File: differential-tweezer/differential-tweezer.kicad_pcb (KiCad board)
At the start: 4 copper layers, 32 x 23 mm, 64 parts, among them J1 5V, J2 IN+, J3 Conn_Coaxial, J4 IN-, J5 Power, U1 R1283B, U2 OPA810, U3 OPA810, U4 OPA810

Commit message: Revision 2
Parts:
- removed C11: 100nF, Capacitor_SMD:C_0603_1608Metric
- removed C18: 22nF, Capacitor_SMD:C_0603_1608Metric
- removed FID1, FID2, FID3, FID4: Fiducial_0.5mm_Mask1mm, Fiducial:Fiducial_0.5mm_Mask1mm
- removed R8: 470, Resistor_SMD:R_0603_1608Metric
- removed RV3: 47k, Potentiometer_SMD:Potentiometer_Bourns_TC33X_Vertical
- removed SLOT1, SLOT2: SLOT_5x1, oscilloscope-probes:SLOT_5x1
- added C24: 100nF, Capacitor_SMD:C_0603_1608Metric, F.Cu at (88.0, 144.5)
- added C25: 100nF, Capacitor_SMD:C_0603_1608Metric, F.Cu at (94.8, 142.3)
- added C26: 10µF, Capacitor_SMD:C_0603_1608Metric, F.Cu at (78.9, 147.9)
- added H1: 2.2mm, MountingHole:MountingHole_2.2mm_M2_DIN965_Pad, F.Cu at (89.4, 149.7)
- added J6: Probe-, oscilloscope-probes:TE_2306454_LEFT, F.Cu at (72.9, 128.2)
- added L8: 1k, Inductor_SMD:L_0603_1608Metric, F.Cu at (73.3, 136.9)
- added R16: 22, Resistor_SMD:R_0603_1608Metric, F.Cu at (89.7, 125.8)
- added R17: 22, Resistor_SMD:R_0603_1608Metric, F.Cu at (75.8, 127.0)
- added R18: 110, Resistor_SMD:R_0603_1608Metric, F.Cu at (91.3, 118.5)
- added R19: 110, Resistor_SMD:R_0603_1608Metric, F.Cu at (78.1, 118.3)
- added R20: 220, Resistor_SMD:R_0603_1608Metric, F.Cu at (94.8, 143.8)
- added R21: 220, Resistor_SMD:R_0603_1608Metric, F.Cu at (93.7, 146.0)
- added R22: 49.9, Resistor_SMD:R_0603_1608Metric, F.Cu at (87.3, 141.6)
- added SW1: GAIN, oscilloscope-probes:78HF01GWRT, F.Cu at (84.0, 131.2)
- added TP1: +5V, TestPoint:TestPoint_Pad_D2.5mm, B.Cu at (93.9, 148.9)
- added TP2: +6V, TestPoint:TestPoint_Pad_D2.5mm, B.Cu at (81.1, 136.1)
- added TP3: -6V, TestPoint:TestPoint_Pad_D2.5mm, B.Cu at (81.1, 139.7)
- added TP4: GND, TestPoint:TestPoint_Pad_D2.5mm, B.Cu at (78.0, 142.0)
- C1, C12, C2, C9: footprint Capacitor_SMD:C_0805_2012Metric -> Capacitor_SMD:C_0603_1608Metric; moved to F.Cu
- C10: value 10µF -> 100nF; footprint Capacitor_SMD:C_0805_2012Metric -> Capacitor_SMD:C_0603_1608Metric; moved to F.Cu
- C13, C6, C7: value 100nF -> 10µF
- C14, C15: value 100nF -> 20pF
- C16, C17: value 10µF -> 8-30pF; footprint Capacitor_SMD:C_0805_2012Metric -> Capacitor_SMD:C_Trimmer_Murata_TZC3; moved to F.Cu
- C19: value 2pF -> N/A
- C20, C22, C23: value 6pF -> 100nF; footprint Capacitor_SMD:C_Trimmer_Murata_TZC3 -> Capacitor_SMD:C_0603_1608Metric
- C21: value 2pF -> 100nF
- C3: value 100nF -> 10µF; moved to F.Cu
- C4: value 10µF -> 100pF; footprint Capacitor_SMD:C_0805_2012Metric -> Capacitor_SMD:C_0603_1608Metric; moved to F.Cu
- C5: value 100nF -> 100pF
- C8: value 22nF -> 10µF; moved to F.Cu
- D1, D2: value BAT54 -> NSR05T30; footprint Diode_SMD:D_SOD-123 -> Diode_SMD:D_SOD-523; moved to F.Cu
- J1: value 5V -> Triax; footprint oscilloscope-probes:WIREPAD_WIDE -> oscilloscope-probes:TRIAX_TUBE
- J2: value IN+ -> Input; footprint oscilloscope-probes:SOLDERPAD_3x1.5 -> oscilloscope-probes:Tensility_54-00177
- J3: value Conn_Coaxial -> Probe+; footprint oscilloscope-probes:COAX_SOLDER -> oscilloscope-probes:TE_2306454_RIGHT
- J4: value IN- -> Probe+_GND; footprint oscilloscope-probes:SOLDERPAD_3x1.5 -> oscilloscope-probes:TE_2306454_RIGHT
- J5: value Power -> Probe-_GND; footprint Connector_PinHeader_2.54mm:PinHeader_1x04_P2.54mm_Vertical -> oscilloscope-probes:TE_2306454_LEFT
- L1, L5, L6, R1, R4, U1: moved to F.Cu
- L2, L7: value 47µH -> 1k; footprint Inductor_SMD:L_Taiyo-Yuden_NR-40xx_HandSoldering -> Inductor_SMD:L_0603_1608Metric; moved to F.Cu
- L3, L4: value 1k -> 4.7µH; footprint Inductor_SMD:L_0603_1608Metric -> Inductor_SMD:L_0805_2012Metric; moved to F.Cu
- R10, R9: value 1M -> 499k
- R12: value 47 -> 475k
- R13: value 470 -> 475k
- R14: value 470 -> 220
- R15: value 1M -> 220
- R2: value 100k -> 4.99k; moved to F.Cu
- R3: value 10k -> 4.99k; moved to F.Cu
- R5: value 100k -> 1k; moved to F.Cu
- R6: value 10k -> 1k; moved to F.Cu
- R7: value 470 -> 10M
- RV1, RV2: value 47k -> 50k
- U2, U3, U4: value OPA810 -> OPA659; footprint Package_TO_SOT_SMD:SOT-23-5 -> Package_SON:Texas_S-PVSON-N8_ThermalVias
- moved L4 27.7 mm to (73.8, 143.2), turned to 90 degrees
- moved C4 27.2 mm to (77.4, 147.9)
- moved C5 27.1 mm to (76.6, 150.2)
- moved J1 26.1 mm to (84.1, 139.8), turned to 90 degrees
- moved C1 25.0 mm to (94.2, 150.5), turned to 270 degrees
- moved C23 24.6 mm to (75.1, 118.3), turned to 270 degrees
- moved R10 24.2 mm to (80.0, 122.9)
- moved L1 23.2 mm to (95.6, 149.0), turned to 90 degrees
- moved C3 22.4 mm to (90.7, 146.1)
- moved C2 22.1 mm to (92.7, 150.5)
- moved C20 21.2 mm to (89.8, 118.5), turned to 90 degrees
- moved C7 21.0 mm to (75.6, 140.7)
- moved L2 21.0 mm to (93.3, 148.2), turned to 180 degrees
- moved L6 20.4 mm to (75.6, 139.2), turned to 180 degrees
- moved J5 20.1 mm to (73.0, 125.5), turned to 87 degrees
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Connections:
- C1 pad 1: Net-(C1-Pad1) -> +5V
- C10 pad 1: Net-(C10-Pad1) -> /OFFSET_TRIM
- C12 pad 1: -12V -> +6V
- C13 pad 1: GND -> -6V
- C13 pad 2: -12V -> GND
- C14 pad 1: GND -> /IN+
- C14 pad 2: -12V -> /CONN_IN+
- C15 pad 1: GND -> /IN-
- C15 pad 2: -12V -> /CONN_IN-
- C16 pad 1: Net-(C16-Pad1) -> /IN+
- C17 pad 1: Net-(C17-Pad1) -> /IN-
- C19 pad 1: GND -> Net-(C19-Pad1)
- C20 pad 1: Net-(C20-Pad1) -> +6V
- C21 pad 1: Net-(C21-Pad1) -> GND
- C21 pad 2: Net-(C21-Pad2) -> -6V
- C22 pad 1: Net-(C22-Pad1) -> +6V
- C23 pad 1: Net-(C23-Pad1) -> GND
- C23 pad 2: Net-(C21-Pad1) -> -6V
- C3 pad 1: Net-(C2-Pad1) -> Net-(C26-Pad1)
- C4 pad 1: +12V -> Net-(C4-Pad1)
- C4 pad 2: GND -> Net-(C4-Pad2)
- C5 pad 1: +12V -> Net-(C5-Pad1)
- C5 pad 2: GND -> Net-(C5-Pad2)
- C6 pad 1: +12V -> Net-(C6-Pad1)
- C7 pad 1: +12V -> Net-(C7-Pad1)
- C8 pad 2: Net-(C8-Pad2) -> GND
- D1 pad 1: Net-(C1-Pad1) -> Net-(D1-Pad1)
- D1 pad 2: Net-(D1-Pad2) -> Net-(C7-Pad1)
- D2 pad 1: Net-(D2-Pad1) -> Net-(C6-Pad1)
- D2 pad 2: Net-(C9-Pad1) -> Net-(D2-Pad2)
- J1 pad 1: Net-(C16-Pad1) -> /OUT
- J3 pad 1: Net-(C23-Pad1) -> /IN+
- J4 pad 1: Net-(C22-Pad1) -> GND
- J5 pad 1: +12V -> GND
- L1 pad 1: Net-(C16-Pad1) -> +5V
- L1 pad 2: Net-(C17-Pad1) -> Net-(C2-Pad1)
- L2 pad 1: Net-(C17-Pad1) -> Net-(C2-Pad1)
- L2 pad 2: Net-(D1-Pad2) -> Net-(C26-Pad1)
- L3 pad 1: Net-(C1-Pad1) -> Net-(C26-Pad1)
- L3 pad 2: Net-(C2-Pad1) -> Net-(D2-Pad2)
- L4 pad 1: Net-(C2-Pad1) -> GND
- L4 pad 2: +12V -> Net-(D1-Pad1)
- L5 pad 1: Net-(C9-Pad1) -> Net-(C6-Pad1)
- L5 pad 2: Net-(C10-Pad1) -> Net-(C8-Pad1)
- L6 pad 1: Net-(C10-Pad1) -> Net-(C7-Pad1)
- L6 pad 2: -12V -> Net-(C9-Pad1)
- L7 pad 1: GND -> Net-(C8-Pad1)
- L7 pad 2: Net-(D2-Pad1) -> +6V
- R1 pad 1: Net-(C8-Pad1) -> Net-(C5-Pad2)
- R1 pad 2: Net-(C1-Pad1) -> Net-(R1-Pad2)
- R10 pad 1: Net-(R10-Pad1) -> /IN-
- R10 pad 2: Net-(C23-Pad1) -> /CONN_IN-
- R12 pad 1: Net-(C23-Pad1) -> /IN+
- R12 pad 2: Net-(C21-Pad1) -> Net-(R12-Pad2)
- R13 pad 1: Net-(R13-Pad1) -> /IN-
- R13 pad 2: Net-(C21-Pad2) -> Net-(R13-Pad2)
- R14 pad 1: Net-(C21-Pad2) -> Net-(R14-Pad1)
- R14 pad 2: Net-(C21-Pad1) -> Net-(R14-Pad2)
- R15 pad 1: Net-(C22-Pad1) -> Net-(R15-Pad1)
- R2 pad 1: Net-(C1-Pad1) -> Net-(C6-Pad1)
- R2 pad 2: Net-(C8-Pad2) -> Net-(C4-Pad2)
- R3 pad 1: GND -> Net-(C7-Pad1)
- R3 pad 2: Net-(C8-Pad2) -> Net-(C5-Pad2)
- R4 pad 1: Net-(C18-Pad1) -> Net-(C4-Pad1)
- R4 pad 2: Net-(C9-Pad1) -> Net-(C6-Pad1)
- R5 pad 1: Net-(C9-Pad1) -> Net-(C5-Pad1)
- R5 pad 2: Net-(C18-Pad2) -> Net-(C7-Pad1)
- R6 pad 1: Net-(C18-Pad2) -> GND
- R6 pad 2: Net-(R6-Pad2) -> Net-(C4-Pad2)
- R7 pad 1: Net-(R7-Pad1) -> /OFFSET_TRIM
- R7 pad 2: Net-(C19-Pad2) -> Net-(R12-Pad2)
- R9 pad 1: Net-(C20-Pad1) -> /IN+
- R9 pad 2: Net-(R9-Pad2) -> /CONN_IN+
- RV1 pad 1: +12V -> Net-(R12-Pad2)
- RV1 pad 2: Net-(R10-Pad1) -> GND
- RV1 pad 3: -12V -> Net-(R13-Pad2)
- RV2 pad 1: Net-(R9-Pad2) -> +6V
- RV2 pad 2: GND -> /OFFSET_TRIM
- RV2 pad 3: GND -> -6V
- U1 pad 11: Net-(C17-Pad1) -> Net-(C26-Pad1)
- U1 pad 2: Net-(D1-Pad2) -> Net-(D2-Pad2)
- U1 pad 3: Net-(D2-Pad1) -> Net-(D1-Pad1)
- U1 pad 5: Net-(C17-Pad1) -> Net-(C26-Pad1)
- U1 pad 6: Net-(C18-Pad2) -> Net-(C5-Pad2)
- U1 pad 7: Net-(R6-Pad2) -> Net-(R1-Pad2)
- U1 pad 8: Net-(C17-Pad1) -> Net-(C26-Pad1)
- U1 pad 9: Net-(C8-Pad2) -> Net-(C4-Pad2)
- U2 pad 1: Net-(R7-Pad1) -> Net-(U2-Pad1)
- U2 pad 2: -12V -> Net-(R14-Pad2)
- U2 pad 3: Net-(C20-Pad1) -> /IN+
- U2 pad 4: Net-(R7-Pad1) -> -6V
- U2 pad 5: +12V -> Net-(U2-Pad5)
- U3 pad 1: Net-(C21-Pad1) -> Net-(U3-Pad1)
- U3 pad 2: -12V -> Net-(R15-Pad1)
- U3 pad 3: Net-(C19-Pad2) -> /IN-
- U3 pad 4: Net-(C21-Pad2) -> -6V
- U3 pad 5: +12V -> Net-(U3-Pad5)
- U4 pad 1: Net-(R13-Pad1) -> Net-(U4-Pad1)
- U4 pad 2: -12V -> Net-(C19-Pad2)
- U4 pad 3: Net-(C22-Pad1) -> Net-(R18-Pad2)
- U4 pad 4: Net-(R13-Pad1) -> -6V
- U4 pad 5: +12V -> Net-(U4-Pad5)
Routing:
- net GND: track 131.9 -> 34.9 mm, vias 31 -> 24
- net -12V: track 50.4 -> 0.00 mm
- net +12V: track 40.2 -> 0.00 mm, vias 4 -> 0
- net Net-(C17-Pad1): track 38.1 -> 0.00 mm, vias 6 -> 0
- net Net-(R18-Pad2): track 0.00 -> 37.3 mm, vias 0 -> 2
- net Net-(C19-Pad2): track 7.11 -> 41.2 mm, vias 0 -> 2
- net Net-(C26-Pad1): track 0.00 -> 33.1 mm, vias 0 -> 3
- net Net-(C21-Pad1): track 20.4 -> 0.00 mm
- net Net-(C10-Pad1): track 19.3 -> 0.00 mm, vias 2 -> 0
- net Net-(C2-Pad1): track 20.7 -> 3.57 mm, vias 2 -> 0
- net Net-(C6-Pad1): track 0.00 -> 16.2 mm, vias 0 -> 2
- net Net-(C7-Pad1): track 0.00 -> 16.0 mm
- net Net-(D1-Pad2): track 15.4 -> 0.00 mm
- net Net-(D2-Pad1): track 15.3 -> 0.00 mm
- net -6V: track 0.00 -> 14.6 mm, vias 0 -> 2
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- added copper zone on In2.Cu, net +6V
- added copper zone on B.Cu, net -6V
- removed copper zone on F.Cu, net GND
- removed copper zone on In2.Cu, net GND
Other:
- board size 32 x 23 mm -> 25.6 x 37 mm
- rule pad_to_mask_clearance: 0.05 -> 0
- board text added: "Diff. amp devEmbedded Rev 2, 5/2021"
- board text added: "Enclosure front edge"
- board text removed: "+12V"
- board text removed: "+5V"
- board text removed: "-12V"
- board text removed: "Diff. Amp"
- board text removed: "GND"
- board text removed: "JLCJLCJLCJLC"
- board text removed: "Rev 1 01/2021"

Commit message: Revision 3
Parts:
- removed C14, C15: 20pF, Capacitor_SMD:C_0603_1608Metric
- removed R4, R5: 1k, Resistor_SMD:R_0603_1608Metric
- added C11: 3pF, Capacitor_SMD:C_0603_1608Metric, F.Cu at (75.8, 125.7)
- added D3: RED, LED_SMD:LED_0603_1608Metric, F.Cu at (93.7, 150.6)
- added D4: PESD5V0X1B, Package_TO_SOT_SMD:SOT-23, F.Cu at (93.6, 121.1)
- added D5: PESD5V0X1B, Package_TO_SOT_SMD:SOT-23, F.Cu at (74.4, 121.2)
- added D6: PESD5V0X1B, Package_TO_SOT_SMD:SOT-23, F.Cu at (88.0, 143.3)
- added J7: IN+, oscilloscope-probes:RF11-27A-T-00-50-G, F.Cu at (88.3, 118.9)
- added J8: IN-, oscilloscope-probes:RF11-27A-T-00-50-G, F.Cu at (79.7, 118.9)
- added L9: MMZ1608B601, Inductor_SMD:L_0603_1608Metric, F.Cu at (80.2, 147.4)
- added R11: 110, Resistor_SMD:R_0603_1608Metric, F.Cu at (75.8, 127.2)
- added R23: 110, Resistor_SMD:R_0603_1608Metric, F.Cu at (92.2, 124.2)
- added R8: 5.1k, Resistor_SMD:R_0603_1608Metric, F.Cu at (93.7, 149.1)
- C1: value 10µF -> 3pF
- C19: value N/A -> 3pF
- J1: value Triax -> Triax_inner; footprint oscilloscope-probes:TRIAX_TUBE -> oscilloscope-probes:COAX_2MM
- J2: value Input -> Triax_outer; footprint oscilloscope-probes:Tensility_54-00177 -> oscilloscope-probes:TRIAX_OUTER_3MM
- J3: value Probe+ -> Spring+S
- J4: value Probe+_GND -> Spring+G
- J5: value Probe-_GND -> Spring-G
- J6: value Probe- -> Spring-S
- L1, L2, L5, L6, L7, L8: value 1k -> MMZ1608B601
- L3, L4: footprint Inductor_SMD:L_0805_2012Metric -> Inductor_SMD:L_0805_2012Metric_Pad1.15x1.40mm_HandSolder
- R10, R9: value 499k -> 49.9
- R12, R13: value 475k -> 487k
- R16, R17: value 22 -> 24
- R2, R3: value 4.99k -> 5.1k
- R7: value 10M -> 5.1k
- RV1, RV2: value 50k -> 20k
- U1: value R1283B -> R1283K001C
- moved R19 27.7 mm to (94.2, 140.8), turned to 180 degrees
- moved J2 27.4 mm to (84.0, 148.4), turned to 90 degrees
- moved C1 24.9 mm to (92.2, 125.7), turned to 0 degrees
- moved R18 22.3 mm to (91.2, 140.8), turned to 180 degrees
- moved C23 15.9 mm to (89.9, 123.9)
- moved L1 15.5 mm to (80.2, 150.4)
- moved L2 15.4 mm to (78.0, 149.8), turned to 0 degrees
- moved C2 14.7 mm to (78.0, 151.3), turned to 180 degrees
- moved C21 13.8 mm to (79.7, 123.0), turned to 0 degrees
- moved C3 12.7 mm to (78.0, 146.8), turned to 180 degrees
- moved C22 10.5 mm to (83.9, 125.9), turned to 270 degrees
- moved TP1 10.1 mm to (84.0, 147.0)
- moved TP3 7.41 mm to (88.0, 137.0)
- moved C20 7.32 mm to (84.0, 122.9)
- moved C24 7.26 mm to (94.8, 146.8), turned to 0 degrees
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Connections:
- C1 pad 1: +5V -> Net-(C1-Pad1)
- C1 pad 2: GND -> Net-(C1-Pad2)
- C10 pad 2: GND -> GNDA
- C12 pad 2: GND -> GNDA
- C13 pad 2: GND -> GNDA
- C16 pad 2: GND -> GNDA
- C17 pad 2: GND -> GNDA
- C20 pad 2: GND -> GNDA
- C21 pad 1: GND -> GNDA
- C22 pad 2: GND -> GNDA
- C23 pad 1: GND -> GNDA
- C24 pad 2: GND -> GNDA
- C25 pad 1: GND -> GNDA
- C6 pad 1: Net-(C6-Pad1) -> Net-(C4-Pad1)
- C7 pad 1: Net-(C7-Pad1) -> Net-(C5-Pad1)
- D1 pad 2: Net-(C7-Pad1) -> Net-(C5-Pad1)
- D2 pad 1: Net-(C6-Pad1) -> Net-(C4-Pad1)
- H1 pad 1: GND -> GNDA
- J1 pad 2: GND -> GNDA
- J4 pad 1: GND -> GNDA
- J5 pad 1: GND -> GNDA
- L5 pad 1: Net-(C6-Pad1) -> Net-(C4-Pad1)
- L6 pad 1: Net-(C7-Pad1) -> Net-(C5-Pad1)
- R14 pad 1: Net-(R14-Pad1) -> Net-(C1-Pad2)
- R14 pad 2: Net-(R14-Pad2) -> Net-(C1-Pad1)
- R15 pad 1: Net-(R15-Pad1) -> Net-(C11-Pad2)
- R16 pad 1: Net-(R16-Pad1) -> Net-(C1-Pad1)
- R16 pad 2: Net-(R14-Pad2) -> Net-(R16-Pad2)
- R17 pad 1: Net-(R17-Pad1) -> Net-(C11-Pad2)
- R17 pad 2: Net-(R15-Pad1) -> Net-(R17-Pad2)
- R18 pad 1: Net-(R14-Pad1) -> Net-(C1-Pad2)
- R2 pad 1: Net-(C6-Pad1) -> Net-(C4-Pad1)
- R20 pad 2: GND -> GNDA
- R3 pad 1: Net-(C7-Pad1) -> Net-(C5-Pad1)
- R7 pad 2: Net-(R12-Pad2) -> /OUT
- RV1 pad 2: GND -> GNDA
- SW1 pad 1: Net-(R17-Pad1) -> Net-(R17-Pad2)
- SW1 pad 2: Net-(R16-Pad1) -> Net-(R16-Pad2)
- TP4 pad 1: GND -> GNDA
- U2 pad 2: Net-(R14-Pad2) -> Net-(C1-Pad1)
- U2 pad 3: /IN+ -> Net-(R23-Pad1)
- U2 pad 6: Net-(R14-Pad1) -> Net-(C1-Pad2)
- U3 pad 2: Net-(R15-Pad1) -> Net-(C11-Pad2)
- U3 pad 3: /IN- -> Net-(R11-Pad1)
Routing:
- net -6V: track 14.6 -> 75.5 mm, vias 2 -> 47
- net GNDA: track 0.00 -> 51.1 mm, vias 0 -> 14
- net +6V: track 13.9 -> 64.5 mm
- net Net-(C19-Pad2): track 41.2 -> 5.42 mm, vias 2 -> 0
- net Net-(R18-Pad2): track 37.3 -> 3.06 mm, vias 2 -> 0
- net Net-(C1-Pad2): track 0.00 -> 33.9 mm, vias 0 -> 2
- net Net-(C11-Pad1): track 9.67 -> 32.9 mm, vias 0 -> 3
- net Net-(C6-Pad1): track 16.2 -> 0.00 mm, vias 2 -> 0
- net Net-(C7-Pad1): track 16.0 -> 0.00 mm
- net Net-(C4-Pad1): track 3.65 -> 19.5 mm, vias 0 -> 2
- net Net-(C26-Pad1): track 33.1 -> 20.7 mm
- net Net-(C5-Pad1): track 3.77 -> 13.0 mm
- net /OFFSET_TRIM: track 3.18 -> 10.5 mm
- net /OUT: track 6.55 -> 13.5 mm
- net Net-(R14-Pad1): track 6.41 -> 0.00 mm
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- added copper zone on F.Cu, net -6V
- added copper zone on In1.Cu, net -6V
- added copper zone on In2.Cu, net GND
- added copper zone on In2.Cu, net GNDA
- removed copper zone on In2.Cu, net +6V
- removed copper zone on In1.Cu, net GND
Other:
- board text added: "DEDP-100 Rev 3, 6/2021"
- board text added: "Main pcb front edge"
- board text removed: "Diff. amp devEmbedded Rev 2, 5/2021"
- board text removed: "Enclosure front edge"

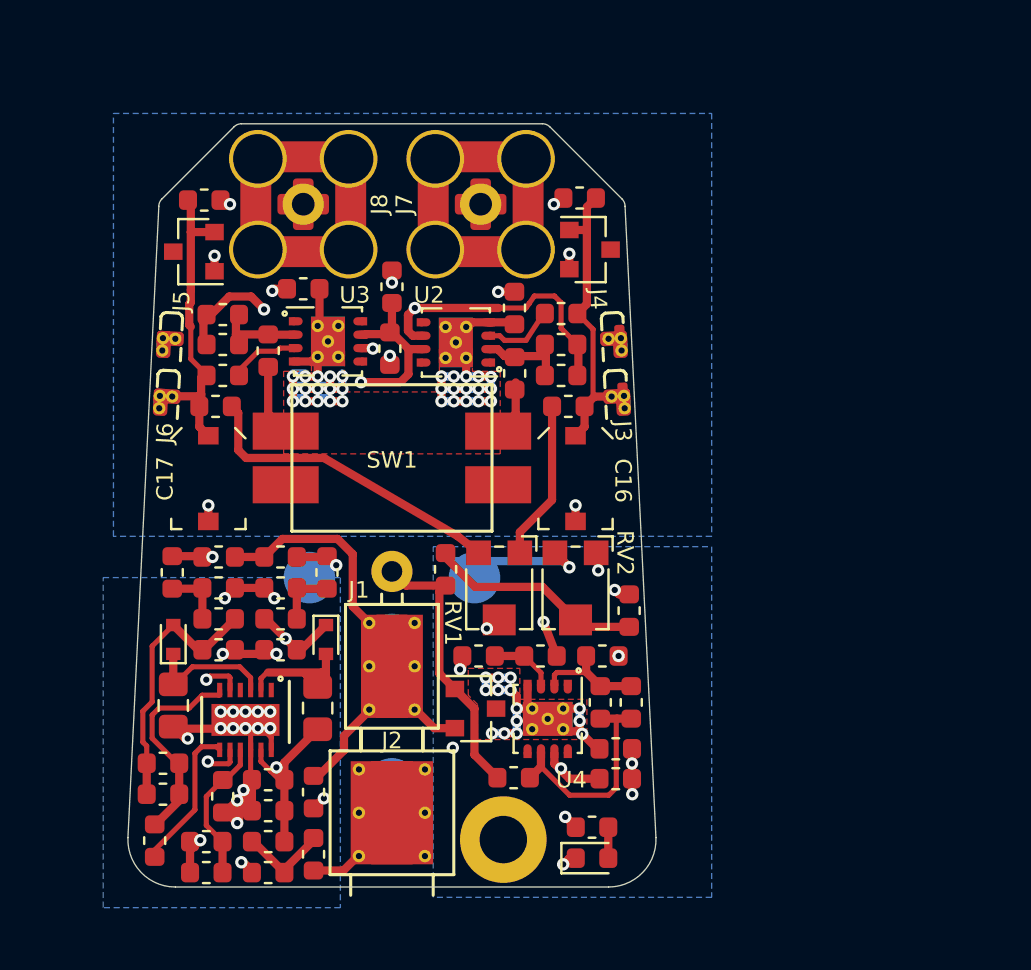
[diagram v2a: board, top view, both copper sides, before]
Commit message: Beginnings of manual
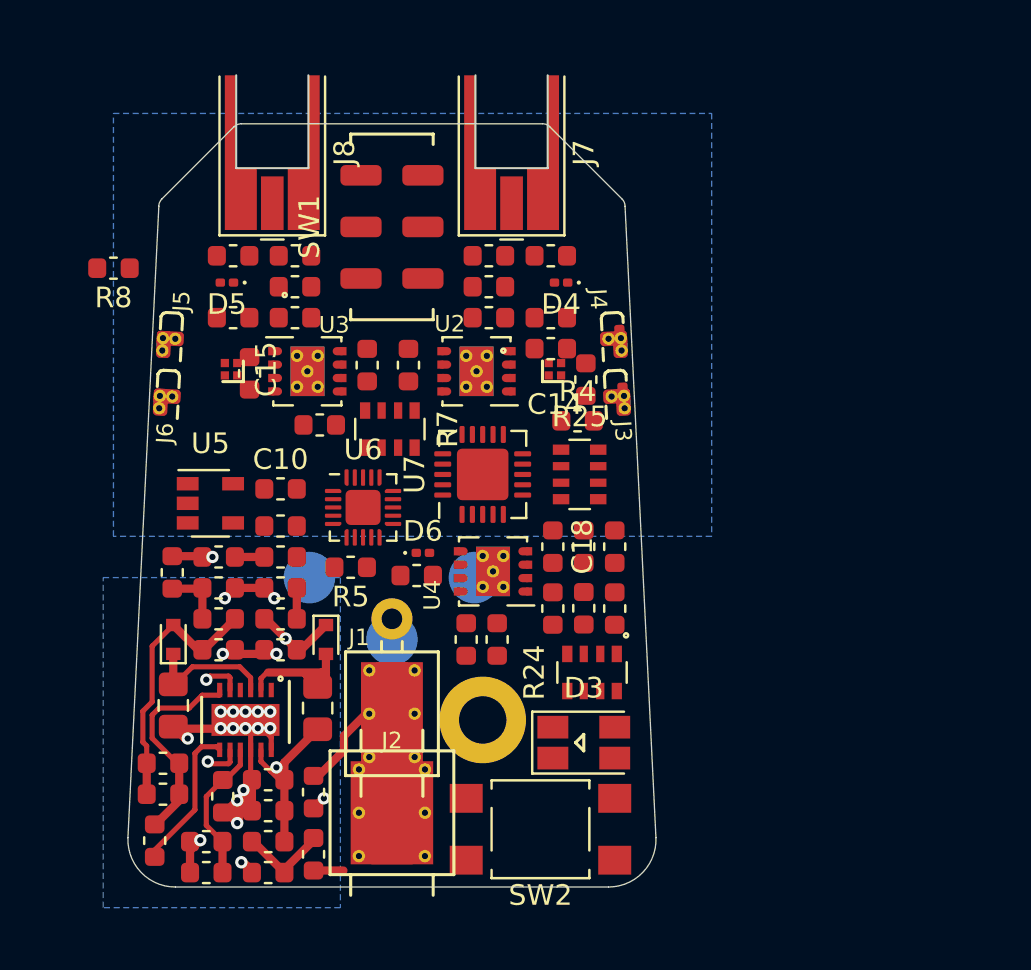
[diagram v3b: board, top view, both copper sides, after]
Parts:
- removed C16, C17: 8-30pF, Capacitor_SMD:C_Trimmer_Murata_TZC3
- removed RV1, RV2: 20k, Potentiometer_SMD:Potentiometer_Bourns_TC33X_Vertical
- added C14: LXRW, oscilloscope-probes:LXRW, F.Cu at (91.9, 126.9)
- added C15: LXRW, oscilloscope-probes:LXRW, F.Cu at (76.2, 126.9)
- added C18: 6pF, Capacitor_SMD:C_0603_1608Metric, F.Cu at (91.8, 135.5)
- added R24: 6.8k, Resistor_SMD:R_Array_Convex_4x0603, F.Cu at (93.7, 141.6)
- added R25: 6.8k, Resistor_SMD:R_Array_Convex_4x0603, F.Cu at (93.1, 132.0)
- added R4: 5.1k, Resistor_SMD:R_0603_1608Metric, F.Cu at (93.0, 129.4)
- added R5: 5.1k, Resistor_SMD:R_0603_1608Metric, F.Cu at (82.0, 136.5)
- added SW2: Calibrate, Button_Switch_SMD:SW_SPST_TL3305A, F.Cu at (91.2, 149.2)
- added U5: MIC5225-5.0YM5, Package_TO_SOT_SMD:SOT-23-5, F.Cu at (75.2, 133.4)
- added U6: ATtiny826-M, Package_DFN_QFN:VQFN-20-1EP_3x3mm_P0.4mm_EP1.7x1.7mm, F.Cu at (82.6, 133.6)
- added U7: MCP4451, Package_DFN_QFN:QFN-20-1EP_4x4mm_P0.5mm_EP2.5x2.5mm, F.Cu at (88.4, 132.0)
- C1, C11, C19: value 3pF -> 6pF
- C10: value 100nF -> 10µF
- C4, C5: value 100pF -> 68pF
- D3: value RED -> APBD3224; footprint LED_SMD:LED_0603_1608Metric -> oscilloscope-probes:APBD3224
- D4, D5, D6: value PESD5V0X1B -> PESD5V0H1BSF; footprint Package_TO_SOT_SMD:SOT-23 -> Diode_SMD:D_0201_0603Metric
- J7, J8: footprint oscilloscope-probes:RF11-27A-T-00-50-G -> Connector_Coaxial:MMCX_Molex_73415-0961_Horizontal_1.6mm-PCB
- R7: value 5.1k -> 6.8k; footprint Resistor_SMD:R_0603_1608Metric -> Resistor_SMD:R_Array_Convex_4x0603
- R8: value 5.1k -> 30k
- SW1: footprint oscilloscope-probes:78HF01GWRT -> oscilloscope-probes:JS202011JCQN
- moved R8 35.7 mm to (70.5, 122.0)
- moved C10 17.9 mm to (78.6, 132.7), turned to 0 degrees
- moved SW1 11.2 mm to (84.0, 120.0), turned to 270 degrees
- moved R22 10.9 mm to (85.2, 136.9)
- moved C24 9.91 mm to (87.6, 140.0), turned to 270 degrees
- moved D6 7.97 mm to (85.5, 135.8)
- moved C25 7.82 mm to (89.1, 140.0), turned to 90 degrees
- moved U4 7.63 mm to (88.9, 136.7), turned to 180 degrees
- moved R20 7.36 mm to (93.3, 135.5), turned to 90 degrees
- moved R7 7.32 mm to (83.9, 129.8)
- moved C21 6.65 mm to (80.5, 129.6), turned to 180 degrees
- moved R18 6.41 mm to (94.8, 135.5), turned to 270 degrees
- moved C19 5.93 mm to (91.8, 138.5)
- moved H1 5.89 mm to (88.4, 143.9)
- moved R16 5.84 mm to (88.7, 121.4), turned to 180 degrees
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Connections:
- C10 pad 1: /OFFSET_TRIM -> +5VA
- D3 pad 1: GNDA -> Net-(D3-Pad1)
- R7 pad 1: /OFFSET_TRIM -> Net-(R12-Pad2)
- R7 pad 2: /OUT -> /DC_CMRR2
- R8 pad 1: Net-(D3-Pad2) -> Net-(C1-Pad1)
- R8 pad 2: +6V -> Net-(C11-Pad2)
- SW1 pad 1: Net-(R17-Pad2) -> Net-(SW1-Pad1)
- SW1 pad 2: Net-(R16-Pad2) -> Net-(R17-Pad2)
- SW1 pad 3: (no net) -> Net-(R16-Pad2)
- SW1 pad 4: (no net) -> Net-(SW1-Pad4)
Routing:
- net +6V: track 64.5 -> 0.00 mm, vias 5 -> 0
- net -6V: track 75.5 -> 16.9 mm, vias 47 -> 1
- net GNDA: track 51.1 -> 5.90 mm, vias 14 -> 0
- net Net-(C1-Pad2): track 33.9 -> 0.00 mm, vias 2 -> 0
- net Net-(C11-Pad1): track 32.9 -> 0.00 mm, vias 3 -> 0
- net /IN-: track 15.4 -> 0.00 mm
- net Net-(R13-Pad2): track 15.4 -> 0.00 mm
- net /IN+: track 14.9 -> 0.00 mm
- net /OUT: track 13.5 -> 0.00 mm
- net Net-(C19-Pad1): track 10.8 -> 0.00 mm
- net /OFFSET_TRIM: track 10.5 -> 0.00 mm
- net Net-(R12-Pad2): track 7.75 -> 0.00 mm
- net +5V: track 9.16 -> 1.45 mm
- net Net-(C19-Pad2): track 5.42 -> 0.00 mm
- net Net-(C1-Pad1): track 4.51 -> 0.00 mm
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- removed copper zone on F.Cu, net -6V
- removed copper zone on In1.Cu, net -6V
- removed copper zone on In2.Cu, net GNDA
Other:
- board text added: "Enclosure front edge"
